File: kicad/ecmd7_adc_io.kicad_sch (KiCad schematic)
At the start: 32 parts, among them U2 MCP33151-05T-E/MN, U4 MCP33151-05T-E/MN, U5 MCP33151-05T-E/MN, U7 MCP33151-05T-E/MN

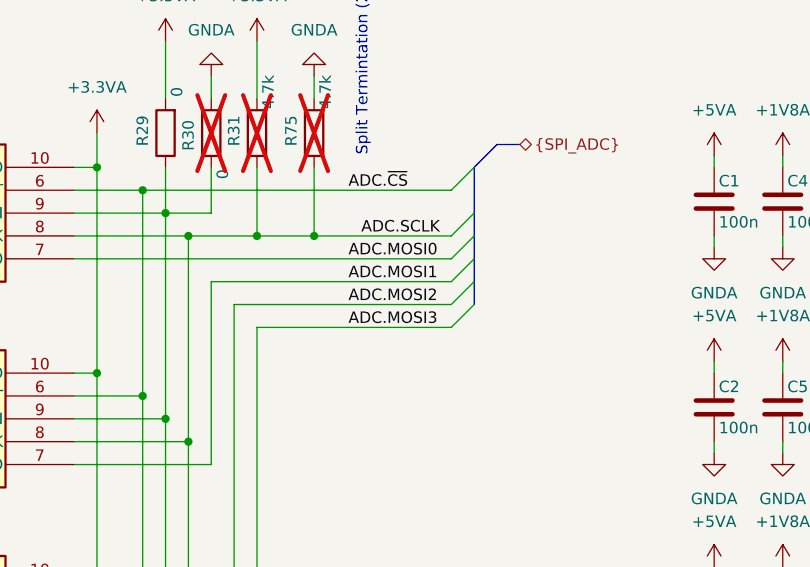
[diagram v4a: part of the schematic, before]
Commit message: Fix MOSI/MISO naming ADC
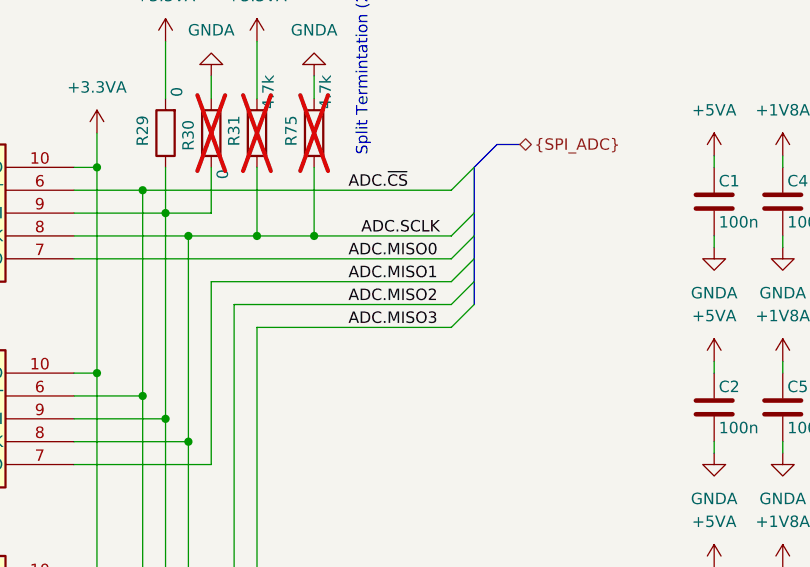
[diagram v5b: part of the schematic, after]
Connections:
- net ADC.MOSI0 renamed ADC.MISO0
- net ADC.MOSI1 renamed ADC.MISO1
- net ADC.MOSI2 renamed ADC.MISO2
- net ADC.MOSI3 renamed ADC.MISO3
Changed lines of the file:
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@@
 		)
 	)
-	(label "ADC.MOSI2"
+	(label "ADC.MISO2"
 		(at 243.84 109.22 0)
 		(effects
@@
 		)
 	)
-	(label "ADC.MOSI3"
+	(label "ADC.MISO3"
 		(at 243.84 111.76 0)
 		(effects
@@
 		)
 	)
-	(label "ADC.MOSI0"
+	(label "ADC.MISO0"
 		(at 243.84 104.14 0)
 		(effects
@@
 		)
 	)
-	(label "ADC.MOSI1"
+	(label "ADC.MISO1"
 		(at 243.84 106.68 0)
 		(effects
